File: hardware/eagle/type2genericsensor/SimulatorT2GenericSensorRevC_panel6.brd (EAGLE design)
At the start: 99.1 x 96.5 mm, 73 parts, among them U1A 2SS52MOFFSET, U1A_1 2SS52MOFFSET, U1A_2 2SS52MOFFSET, U1A_3 2SS52MOFFSET, U1A_4 2SS52MOFFSET, U1A_5 2SS52MOFFSET, U1B 2SS52MOFFSET, U1B_1 2SS52MOFFSET, U1B_2 2SS52MOFFSET, U1B_3 2SS52MOFFSET, U1B_4 2SS52MOFFSET, U1B_5 2SS52MOFFSET

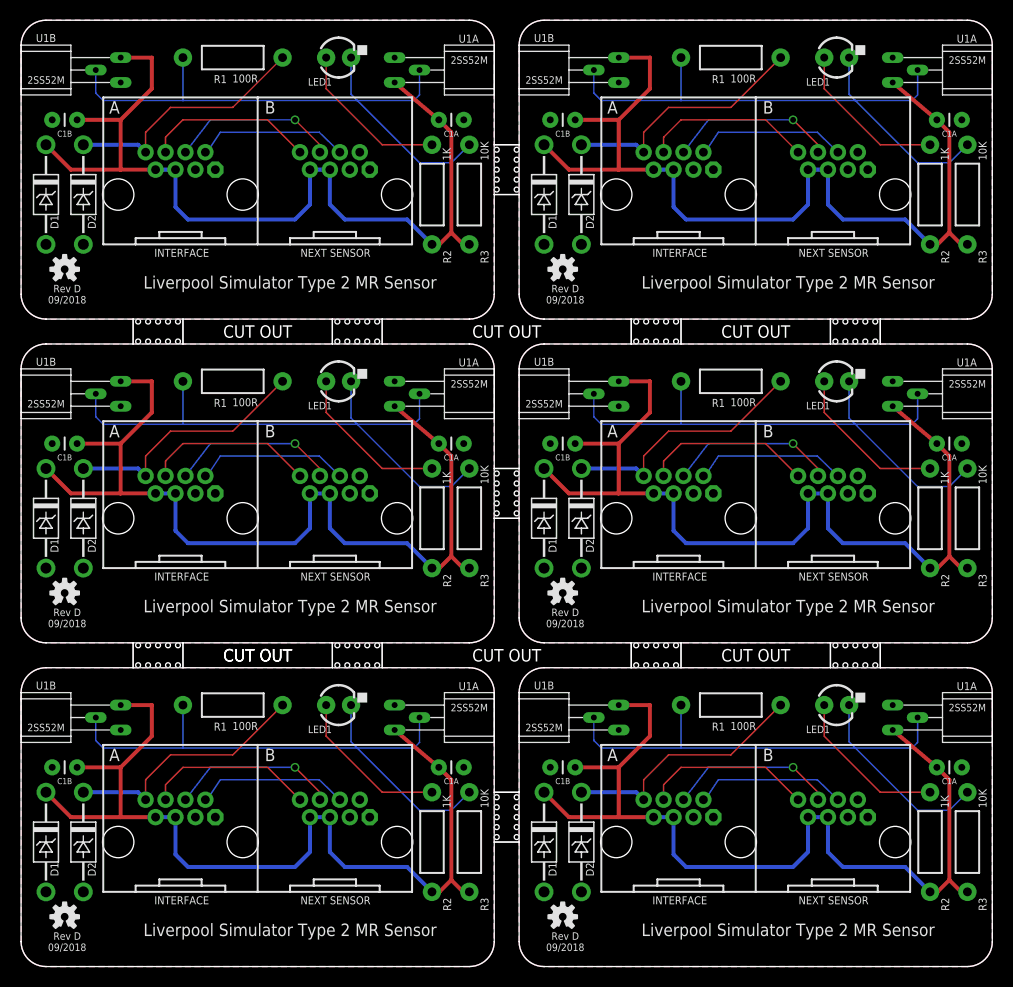
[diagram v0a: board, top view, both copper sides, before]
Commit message: Board Housekeeping
URL on silkscreens, caution messages, tidy up naming conventions.
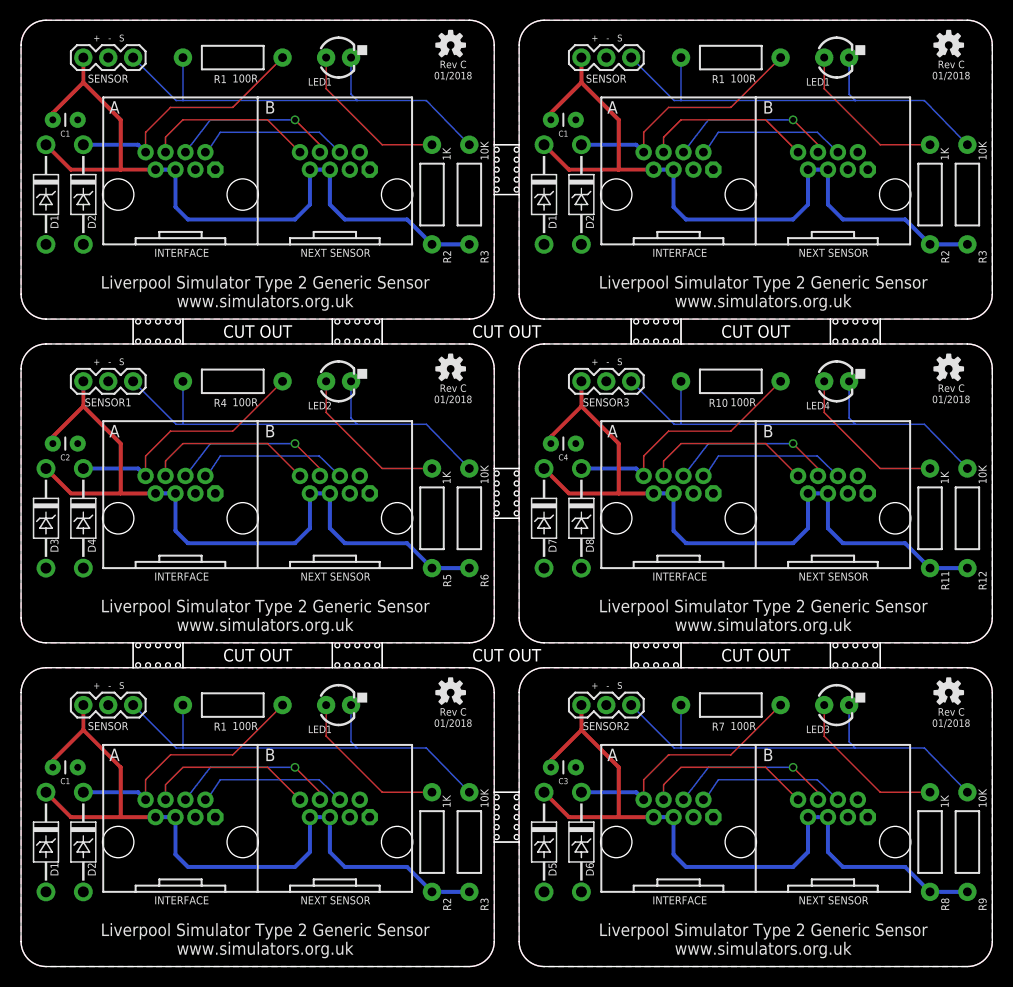
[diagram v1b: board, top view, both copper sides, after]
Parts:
- removed C1A, C1A_1, C1A_2, C1A_3, C1A_4, C1A_5, C1B, C1B_1, C1B_2, C1B_3, C1B_4, C1B_5: 100nF, SparkFun-Passives:CAP-PTH-SMALL
- removed D1_5, D2_5: SA5.0A, AIC_Custom:DO41_TVS_UNI
- removed JP1_5: RJ45-RJHSE-5080-023HOLE, AIC_Custom:RJ45-RJHSE-5080-02-3HOLE
- removed LED1_5: Blue, SparkFun-LED:LED3MM
- removed LOGO1_3, LOGO1_4, LOGO1_5: OSHW-LOGOS, SparkFun-Aesthetics:OSHW-LOGO-S
- removed R1_5: 100R, SparkFun-Passives:AXIAL-0.4
- removed R2_5: 1K, SparkFun-Passives:AXIAL-0.4
- removed R3_5: 10K, SparkFun-Passives:AXIAL-0.4
- removed U1A, U1A_1, U1A_2, U1A_3, U1A_4, U1A_5, U1B, U1B_1, U1B_2, U1B_3, U1B_4, U1B_5: 2SS52MOFFSET, AIC_Custom:2SS52M_FLAT_OFFSET
- added C1, C1_1, C1_2, C2, C3, C4: 100nF, SparkFun-Passives:CAP-PTH-SMALL
- added D3, D4: SA5.0A, AIC_Custom:DO41_TVS_UNI
- added E$2, E$3, E$4, E$5, E$6, E$7: (no value), AIC_Custom:WARNING_TRIANGLE_TPLACE
- added JP2: RJ45-RJHSE-5080-023HOLE, AIC_Custom:RJ45-RJHSE-5080-02-3HOLE
- added LED2: Blue, SparkFun-LED:LED3MM
- added LOGO2, LOGO3, LOGO4: OSHW-LOGOS, SparkFun-Aesthetics:OSHW-LOGO-S
- added R4: 100R, SparkFun-Passives:AXIAL-0.4
- added R5: 1K, SparkFun-Passives:AXIAL-0.4
- added R6: 10K, SparkFun-Passives:AXIAL-0.4
- added SENSOR, SENSOR1, SENSOR2, SENSOR3, SENSOR_1, SENSOR_2: (no value), SparkFun-Connectors:1X03
- moved LOGO1_2 93.0 mm to (94.6, 94.0)
- moved LOGO1_1 68.4 mm to (43.8, 94.0)
- moved JP1_2 50.8 mm to (74.9, 78.7)
- moved D1_2 50.8 mm to (53.3, 78.7)
- moved LED1_2 50.8 mm to (83.2, 92.7)
- moved D2_2 50.8 mm to (57.1, 78.7)
- moved R1_2 50.8 mm to (72.4, 92.7)
- moved R2_2 50.8 mm to (92.7, 78.7)
- moved R3_2 50.8 mm to (96.5, 78.7)
- moved LOGO1 45.5 mm to (43.8, 27.9)
- moved D1_1 33.0 mm to (2.54, 78.7)
- moved D2_1 33.0 mm to (6.35, 78.7)
- moved JP1_1 33.0 mm to (24.1, 78.7)
- moved LED1_1 33.0 mm to (32.4, 92.7)
- moved R1_1 33.0 mm to (21.6, 92.7)
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- renumbered D1_3 to D5, D1_4 to D7, D2_3 to D6, D2_4 to D8, E$12 to E$1, JP1_3 to JP3, JP1_4 to JP4, LED1_3 to LED3, LED1_4 to LED4, R1_3 to R7, R1_4 to R10, R2_3 to R8, R2_4 to R11, R3_3 to R9, R3_4 to R12
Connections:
- net B23 renamed B7
- net B24 renamed B10
- net B33 renamed B8
- net B34 renamed B11
- net B43 renamed B9
- net B44 renamed B12
- removed net B25: JP1_5.A6, JP1_5.B8
- removed net B35: JP1_5.A4, JP1_5.B6
- removed net B45: JP1_5.A2, JP1_5.B4
- new net B1: JP2.A6, JP2.B8
- new net B5: JP2.A4, JP2.B6
- new net B6: JP2.A2, JP2.B4
- net !OUT!1: now also D4.CATHODE, JP2.A8, R4.P$1; no longer D2_1.CATHODE, JP1_1.A8, R1_1.P$1
- net !OUT!2: now also D6.CATHODE, JP3.A8, R7.P$1; no longer D2_2.CATHODE, JP1_2.A8, R1_2.P$1
- net !OUT!3: now also D8.CATHODE, JP4.A8, R10.P$1; no longer D6.CATHODE, JP3.A8, R7.P$1
- net !OUT!4: now also D2_1.CATHODE, JP1_1.A8, R1_1.P$1; no longer D8.CATHODE, JP4.A8, R10.P$1
- net !OUT!5: now also D2_2.CATHODE, JP1_2.A8, R1_2.P$1; no longer D2_5.CATHODE, JP1_5.A8, R1_5.P$1
- net GND: now also C1.2, SENSOR.2; no longer C1A.2, C1B.2, U1A.P$1, U1B.P$1
- net GND1: now also C2.2, D3.ANODE, D4.ANODE, JP2.A1, JP2.A3, JP2.B1, JP2.B3, SENSOR1.2; no longer C1A_1.2, C1B_1.2, D1_1.ANODE, D2_1.ANODE, JP1_1.A1, JP1_1.A3, JP1_1.B1, JP1_1.B3, U1A_1.P$1, U1B_1.P$1
- net GND2: now also C3.2, D5.ANODE, D6.ANODE, JP3.A1, JP3.A3, JP3.B1, JP3.B3, SENSOR2.2; no longer C1A_2.2, C1B_2.2, D1_2.ANODE, D2_2.ANODE, JP1_2.A1, JP1_2.A3, JP1_2.B1, JP1_2.B3, U1A_2.P$1, U1B_2.P$1
- net GND3: now also C4.2, D7.ANODE, D8.ANODE, JP4.A1, JP4.A3, JP4.B1, JP4.B3, SENSOR3.2; no longer C1A_3.2, C1B_3.2, D5.ANODE, D6.ANODE, JP3.A1, JP3.A3, JP3.B1, JP3.B3, U1A_3.P$1, U1B_3.P$1
- net GND4: now also C1_1.2, D1_1.ANODE, D2_1.ANODE, JP1_1.A1, JP1_1.A3, JP1_1.B1, JP1_1.B3, SENSOR_1.2; no longer C1A_4.2, C1B_4.2, D7.ANODE, D8.ANODE, JP4.A1, JP4.A3, JP4.B1, JP4.B3, U1A_4.P$1, U1B_4.P$1
- net GND5: now also C1_2.2, D1_2.ANODE, D2_2.ANODE, JP1_2.A1, JP1_2.A3, JP1_2.B1, JP1_2.B3, SENSOR_2.2; no longer C1A_5.2, C1B_5.2, D1_5.ANODE, D2_5.ANODE, JP1_5.A1, JP1_5.A3, JP1_5.B1, JP1_5.B3, U1A_5.P$1, U1B_5.P$1
- net LED1: now also LED2.A, R5.P$1; no longer LED1_1.A, R2_1.P$1
- net LED2: now also LED3.A, R8.P$1; no longer LED1_2.A, R2_2.P$1
- net LED3: now also LED4.A, R11.P$1; no longer LED3.A, R8.P$1
- net LED4: now also LED1_1.A, R2_1.P$1; no longer LED4.A, R11.P$1
- net LED5: now also LED1_2.A, R2_2.P$1; no longer LED1_5.A, R2_5.P$1
- net SIG: now also SENSOR.3; no longer U1A.P$2, U1B.P$2
- net SIG1: now also LED2.K, R4.P$2, R6.P$1, SENSOR1.3; no longer LED1_1.K, R1_1.P$2, R3_1.P$1, U1A_1.P$2, U1B_1.P$2
- net SIG2: now also LED3.K, R7.P$2, R9.P$1, SENSOR2.3; no longer LED1_2.K, R1_2.P$2, R3_2.P$1, U1A_2.P$2, U1B_2.P$2
- net SIG3: now also LED4.K, R10.P$2, R12.P$1, SENSOR3.3; no longer LED3.K, R7.P$2, R9.P$1, U1A_3.P$2, U1B_3.P$2
- net SIG4: now also LED1_1.K, R1_1.P$2, R3_1.P$1, SENSOR_1.3; no longer LED4.K, R10.P$2, R12.P$1, U1A_4.P$2, U1B_4.P$2
- net SIG5: now also LED1_2.K, R1_2.P$2, R3_2.P$1, SENSOR_2.3; no longer LED1_5.K, R1_5.P$2, R3_5.P$1, U1A_5.P$2, U1B_5.P$2
- net VCC: now also C1.1, SENSOR.1; no longer C1A.1, C1B.1, U1A.P$3, U1B.P$3
- net VCC1: now also C2.1, D3.CATHODE, JP2.A5, JP2.A7, JP2.B5, JP2.B7, R5.P$2, R6.P$2, SENSOR1.1; no longer C1A_1.1, C1B_1.1, D1_1.CATHODE, JP1_1.A5, JP1_1.A7, JP1_1.B5, JP1_1.B7, R2_1.P$2, R3_1.P$2, U1A_1.P$3, U1B_1.P$3
- net VCC2: now also C3.1, D5.CATHODE, JP3.A5, JP3.A7, JP3.B5, JP3.B7, R8.P$2, R9.P$2, SENSOR2.1; no longer C1A_2.1, C1B_2.1, D1_2.CATHODE, JP1_2.A5, JP1_2.A7, JP1_2.B5, JP1_2.B7, R2_2.P$2, R3_2.P$2, U1A_2.P$3, U1B_2.P$3
- net VCC3: now also C4.1, D7.CATHODE, JP4.A5, JP4.A7, JP4.B5, JP4.B7, R11.P$2, R12.P$2, SENSOR3.1; no longer C1A_3.1, C1B_3.1, D5.CATHODE, JP3.A5, JP3.A7, JP3.B5, JP3.B7, R8.P$2, R9.P$2, U1A_3.P$3, U1B_3.P$3
- net VCC4: now also C1_1.1, D1_1.CATHODE, JP1_1.A5, JP1_1.A7, JP1_1.B5, JP1_1.B7, R2_1.P$2, R3_1.P$2, SENSOR_1.1; no longer C1A_4.1, C1B_4.1, D7.CATHODE, JP4.A5, JP4.A7, JP4.B5, JP4.B7, R11.P$2, R12.P$2, U1A_4.P$3, U1B_4.P$3
- net VCC5: now also C1_2.1, D1_2.CATHODE, JP1_2.A5, JP1_2.A7, JP1_2.B5, JP1_2.B7, R2_2.P$2, R3_2.P$2, SENSOR_2.1; no longer C1A_5.1, C1B_5.1, D1_5.CATHODE, JP1_5.A5, JP1_5.A7, JP1_5.B5, JP1_5.B7, R2_5.P$2, R3_5.P$2, U1A_5.P$3, U1B_5.P$3
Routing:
- net VCC5: track 97.3 -> 76.1 mm
- net VCC4: track 97.3 -> 76.1 mm
- net VCC1: track 97.3 -> 76.1 mm
- net VCC: track 97.3 -> 76.1 mm
- net VCC3: track 97.3 -> 76.1 mm
- net VCC2: track 97.3 -> 76.1 mm
- net B1: track 0.00 -> 17.3 mm
- net B25: track 17.3 -> 0.00 mm
- net B5: track 0.00 -> 17.2 mm, vias 0 -> 1
- net B35: track 17.2 -> 0.00 mm, vias 1 -> 0
- net B6: track 0.00 -> 15.6 mm
- net B45: track 15.6 -> 0.00 mm
- net SIG3: track 62.3 -> 47.0 mm
- net SIG4: track 62.3 -> 47.0 mm
- net SIG1: track 62.3 -> 47.0 mm
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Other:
- board text added: "+ - S"
- board text added: "C1"
- board text added: "Connect this board to Liverpool Simulator Type 2 or compatible equipment ONLY. Refer to documentation for details."
- board text added: "Liverpool Simulator Type 2 Generic Sensor www.simulators.org.uk"
- board text added: "Rev C 01/2018"
- board text added: "SENSOR"
- board text removed: "2SS52M Lead Forming Guide"
- board text removed: "C1A"
- board text removed: "C1B"
- board text removed: "CUT OUT"
- board text removed: "Liverpool Simulator Type 2 MR Sensor"
- board text removed: "Rev D 09/2018"
- board text removed: "U1A"
- board text removed: "U1B"
